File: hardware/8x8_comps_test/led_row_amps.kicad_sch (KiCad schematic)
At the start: 5 parts

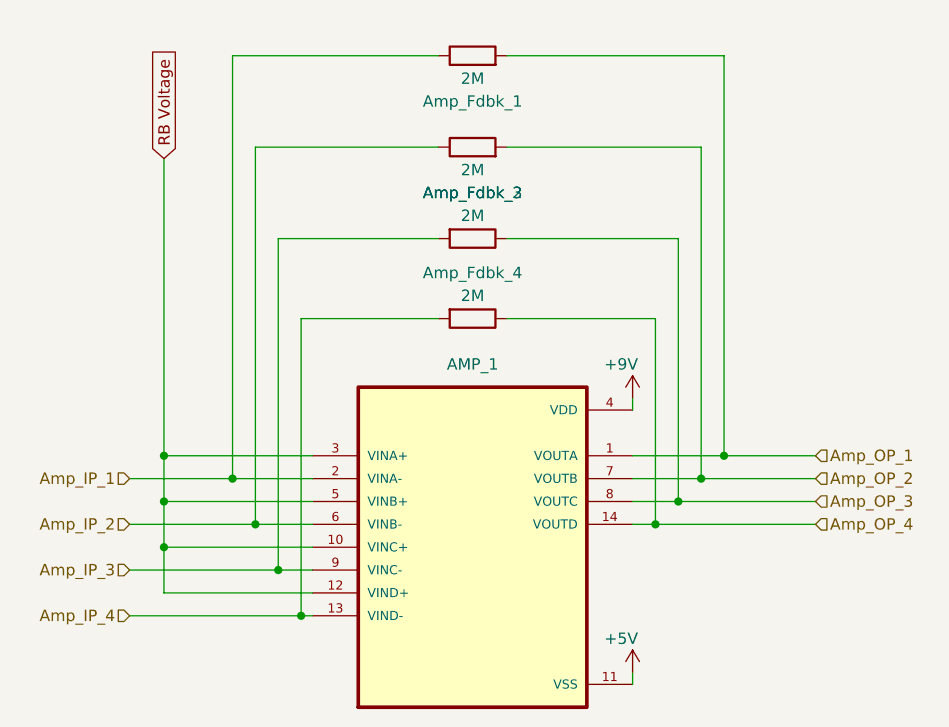
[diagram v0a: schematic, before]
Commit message: Added test Schematic and PCB
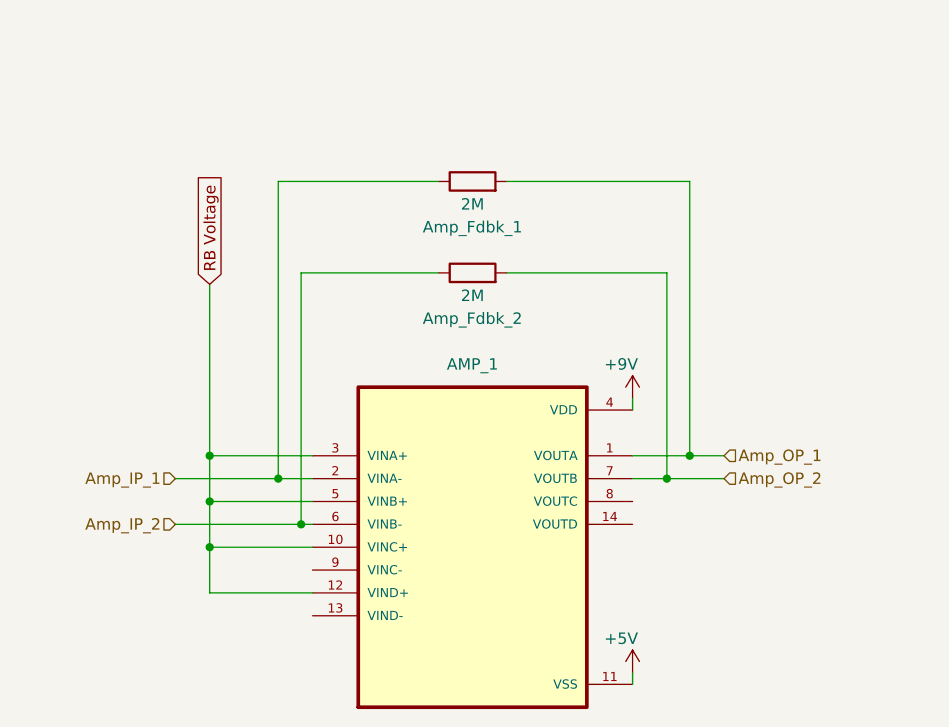
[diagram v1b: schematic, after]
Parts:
- removed Amp_Fdbk_3, Amp_Fdbk_4: 2M, Resistor_THT:R_Axial_DIN0207_L6.3mm_D2.5mm_P7.62mm_Horizontal, symbol Device:R
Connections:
- net Amp_IP_3: no longer names the net of AMP_1.9 (VINC-)
- net Amp_IP_4: no longer names the net of AMP_1.13 (VIND-)
- net Amp_OP_3: no longer names the net of AMP_1.8 (VOUTC)
- net Amp_OP_4: no longer names the net of AMP_1.14 (VOUTD)
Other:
- moved on the sheet: Amp_Fdbk_1, Amp_Fdbk_2

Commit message: Updated PCB
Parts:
- FDB1: renamed from Amp_Fdbk_1; footprint Resistor_THT:R_Axial_DIN0207_L6.3mm_D2.5mm_P7.62mm_Horizontal -> Resistor - Through-Hole:footprints
- FDB2: renamed from Amp_Fdbk_2; footprint Resistor_THT:R_Axial_DIN0207_L6.3mm_D2.5mm_P7.62mm_Horizontal -> Resistor - Through-Hole:footprints
- renumbered AMP_1 to AMP1
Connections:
- net Amp_IP_1: now also AMP1.9 (VINC-); no longer AMP1.2 (VINA-)
- net Amp_OP_1: now also AMP1.8 (VOUTC); no longer AMP1.1 (VOUTA)
- net RB Voltage: no longer AMP1.12 (VIND+), AMP1.3 (VINA+)
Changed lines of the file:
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@@
 (kicad_sch (version 20211123) (generator eeschema)
   (paper "A4")
+  (junction (at 97.79 73.66) (diameter 0) (color 0 0 0 0)
+  )
+  (junction (at 54.61 83.82) (diameter 0) (color 0 0 0 0)
+  )
+  (junction (at 100.33 76.2) (diameter 0) (color 0 0 0 0)
+  )
   (junction (at 57.15 78.74) (diameter 0) (color 0 0 0 0)
-  )
-  (junction (at 54.61 73.66) (diameter 0) (color 0 0 0 0)
   )
   (junction (at 46.99 76.2) (diameter 0) (color 0 0 0 0)
   )
-  (junction (at 46.99 81.28) (diameter 0) (color 0 0 0 0)
+  (wire (pts (xy 57.15 50.8) (xy 57.15 78.74))
+    (stroke (width 0) (type default) (color 0 0 0 0))
   )
-  (junction (at 46.99 71.12) (diameter 0) (color 0 0 0 0)
-  )
-  (junction (at 100.33 71.12) (diameter 0) (color 0 0 0 0)
-  )
-  (junction (at 97.79 73.66) (diameter 0) (color 0 0 0 0)
-  )
-  (wire (pts (xy 57.15 50.8) (xy 57.15 78.74))
+  (wire (pts (xy 58.42 81.28) (xy 46.99 81.28))
     (stroke (width 0) (type default) (color 0 0 0 0))
   )
@@
     (stroke (width 0) (type default) (color 0 0 0 0))
   )
-  (wire (pts (xy 46.99 52.07) (xy 46.99 71.12))
+  (wire (pts (xy 43.18 83.82) (xy 54.61 83.82))
     (stroke (width 0) (type default) (color 0 0 0 0))
   )
-  (wire (pts (xy 54.61 73.66) (xy 58.42 73.66))
-    (stroke (width 0) (type default) (color 0 0 0 0))
-  )
-  (wire (pts (xy 58.42 81.28) (xy 46.99 81.28))
-    (stroke (width 0) (type default) (color 0 0 0 0))
-  )
-  (wire (pts (xy 43.18 73.66) (xy 54.61 73.66))
-    (stroke (width 0) (type default) (color 0 0 0 0))
-  )
-  (wire (pts (xy 93.98 71.12) (xy 100.33 71.12))
+  (wire (pts (xy 80.01 50.8) (xy 97.79 50.8))
     (stroke (width 0) (type default) (color 0 0 0 0))
   )
@@
     (stroke (width 0) (type default) (color 0 0 0 0))
   )
-  (wire (pts (xy 46.99 76.2) (xy 58.42 76.2))
-    (stroke (width 0) (type default) (color 0 0 0 0))
-  )
-  (wire (pts (xy 46.99 71.12) (xy 58.42 71.12))
-    (stroke (width 0) (type default) (color 0 0 0 0))
-  )
-  (wire (pts (xy 80.01 50.8) (xy 97.79 50.8))
-    (stroke (width 0) (type default) (color 0 0 0 0))
-  )
-  (wire (pts (xy 58.42 86.36) (xy 46.99 86.36))
-    (stroke (width 0) (type default) (color 0 0 0 0))
-  )
-  (wire (pts (xy 100.33 71.12) (xy 104.14 71.12))
+  (wire (pts (xy 54.61 83.82) (xy 58.42 83.82))
     (stroke (width 0) (type default) (color 0 0 0 0))
   )
   (wire (pts (xy 93.98 66.04) (xy 93.98 64.77))
+    (stroke (width 0) (type default) (color 0 0 0 0))
+  )
+  (wire (pts (xy 97.79 73.66) (xy 93.98 73.66))
     (stroke (width 0) (type default) (color 0 0 0 0))
   )
@@
     (stroke (width 0) (type default) (color 0 0 0 0))
   )
-  (wire (pts (xy 54.61 73.66) (xy 54.61 40.64))
+  (wire (pts (xy 46.99 76.2) (xy 46.99 81.28))
     (stroke (width 0) (type default) (color 0 0 0 0))
   )
-  (wire (pts (xy 100.33 40.64) (xy 100.33 71.12))
+  (wire (pts (xy 54.61 40.64) (xy 54.61 83.82))
     (stroke (width 0) (type default) (color 0 0 0 0))
   )
-  (wire (pts (xy 93.98 73.66) (xy 97.79 73.66))
+  (wire (pts (xy 97.79 73.66) (xy 104.14 73.66))
     (stroke (width 0) (type default) (color 0 0 0 0))
   )
-  (wire (pts (xy 46.99 71.12) (xy 46.99 76.2))
+  (wire (pts (xy 100.33 40.64) (xy 100.33 76.2))
     (stroke (width 0) (type default) (color 0 0 0 0))
   )
-  (wire (pts (xy 46.99 81.28) (xy 46.99 76.2))
+  (wire (pts (xy 97.79 50.8) (xy 97.79 73.66))
+    (stroke (width 0) (type default) (color 0 0 0 0))
+  )
+  (wire (pts (xy 100.33 76.2) (xy 93.98 76.2))
+    (stroke (width 0) (type default) (color 0 0 0 0))
+  )
+  (wire (pts (xy 46.99 52.07) (xy 46.99 76.2))
     (stroke (width 0) (type default) (color 0 0 0 0))
   )
@@
     (stroke (width 0) (type default) (color 0 0 0 0))
   )
-  (wire (pts (xy 46.99 86.36) (xy 46.99 81.28))
+  (wire (pts (xy 100.33 76.2) (xy 104.14 76.2))
     (stroke (width 0) (type default) (color 0 0 0 0))
   )
-  (wire (pts (xy 97.79 73.66) (xy 104.14 73.66))
-    (stroke (width 0) (type default) (color 0 0 0 0))
-  )
-  (wire (pts (xy 97.79 50.8) (xy 97.79 73.66))
+  (wire (pts (xy 46.99 76.2) (xy 58.42 76.2))
     (stroke (width 0) (type default) (color 0 0 0 0))
   )
@@
     )
   )
-  (hierarchical_label "Amp_IP_1" (shape input) (at 43.18 73.66 180)
+  (hierarchical_label "Amp_IP_1" (shape input) (at 43.18 83.82 180)
     (effects (font (size 1.27 1.27)) (justify right))
   )
@@
     (effects (font (size 1.27 1.27)) (justify right))
   )
-  (hierarchical_label "Amp_OP_1" (shape input) (at 104.14 71.12 0)
+  (hierarchical_label "Amp_OP_1" (shape input) (at 104.14 76.2 0)
     (effects (font (size 1.27 1.27)) (justify left))
   )
@@
   (symbol (lib_id "Device:R") (at 76.2 50.8 90) (unit 1)
     (in_bom yes) (on_board yes)
-    (property "Reference" "Amp_Fdbk_2" (id 0) (at 76.2 55.88 90))
+    (property "Reference" "FDB2" (id 0) (at 76.2 55.88 90))
     (property "Value" "2M" (id 1) (at 76.2 53.34 90))
-    (property "Footprint" "Resistor_THT:R_Axial_DIN0207_L6.3mm_D2.5mm_P7.62mm_Horizontal" (id 2) (at 76.2 52.578 90)
+    (property "Footprint" "Resistor - Through-Hole:footprints" (id 2) (at 76.2 52.578 90)
       (effects (font (size 1.27 1.27)) hide)
     )
@@
   (symbol (lib_id "Device:R") (at 76.2 40.64 90) (unit 1)
     (in_bom yes) (on_board yes)
-    (property "Reference" "Amp_Fdbk_1" (id 0) (at 76.2 45.72 90))
+    (property "Reference" "FDB1" (id 0) (at 76.2 45.72 90))
     (property "Value" "2M" (id 1) (at 76.2 43.18 90))
-    (property "Footprint" "Resistor_THT:R_Axial_DIN0207_L6.3mm_D2.5mm_P7.62mm_Horizontal" (id 2) (at 76.2 42.418 90)
+    (property "Footprint" "Resistor - Through-Hole:footprints" (id 2) (at 76.2 42.418 90)
       (effects (font (size 1.27 1.27)) hide)
     )
@@
   (symbol (lib_id "Op-Amp:MCP619-I{brace}slash}SL") (at 76.2 81.28 0) (unit 1)
     (in_bom yes) (on_board yes) (fields_autoplaced)
-    (property "Reference" "AMP_1" (id 0) (at 76.2 60.96 0))
+    (property "Reference" "AMP1" (id 0) (at 76.2 60.96 0))
     (property "Value" "MCP619-I{slash}SL" (id 1) (at 76.2 60.96 0)
       (effects (font (size 1.27 1.27)) hide)
